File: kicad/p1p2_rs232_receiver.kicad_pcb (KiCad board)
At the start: 2 copper layers, 49 x 24.8 mm, 43 parts, among them J101 Conn_01x03_Female, J102 Conn_01x10_Female, U101 NCP1117-3.3_SOT223, U102 TEC2-1211WI, U103 LM4861

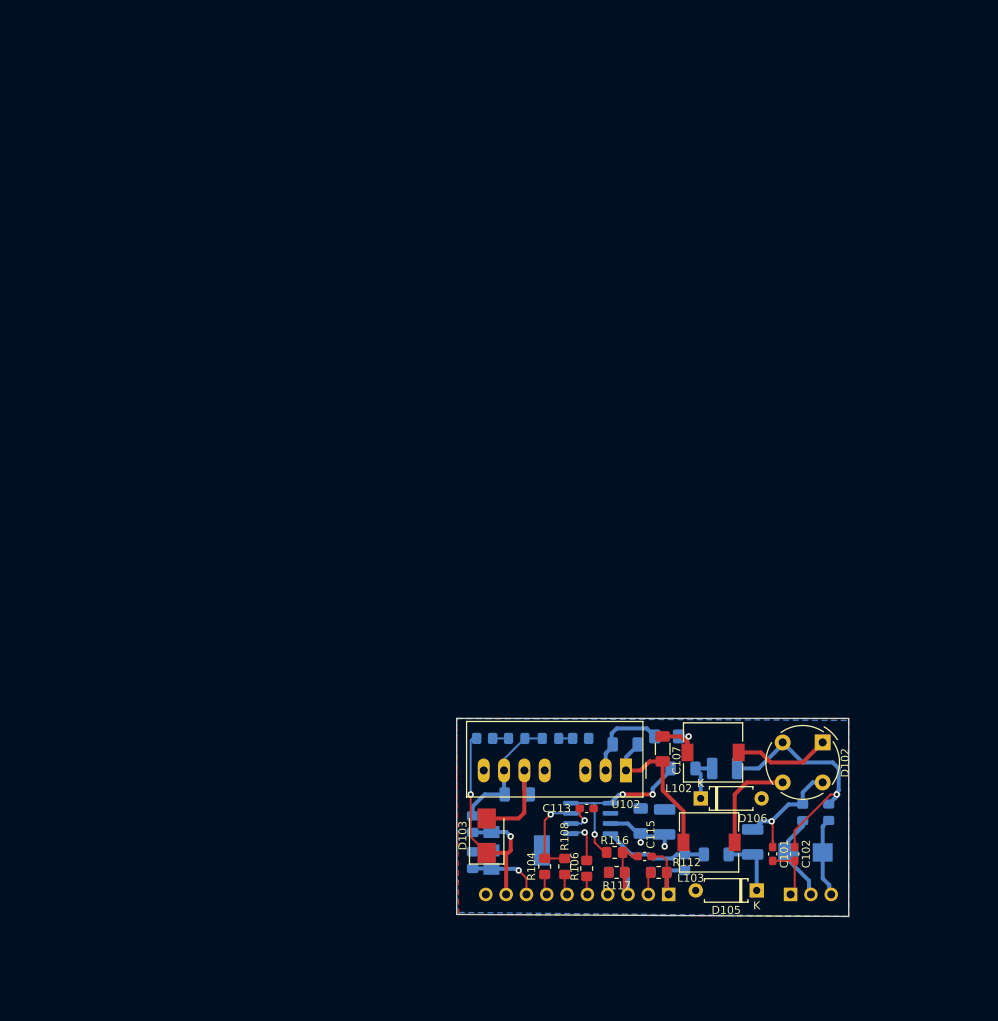
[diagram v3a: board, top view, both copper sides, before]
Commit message: kicad: Create a PI hat compatible P1/P2 modem
Create a P1/P2 transceiver as Rapsberry PI hat using some
analog components and a Raspberry PI Pico (RP2040).

Signed-off-by: Patrick Rudolph <rudolphpatrick05@gmail.com>
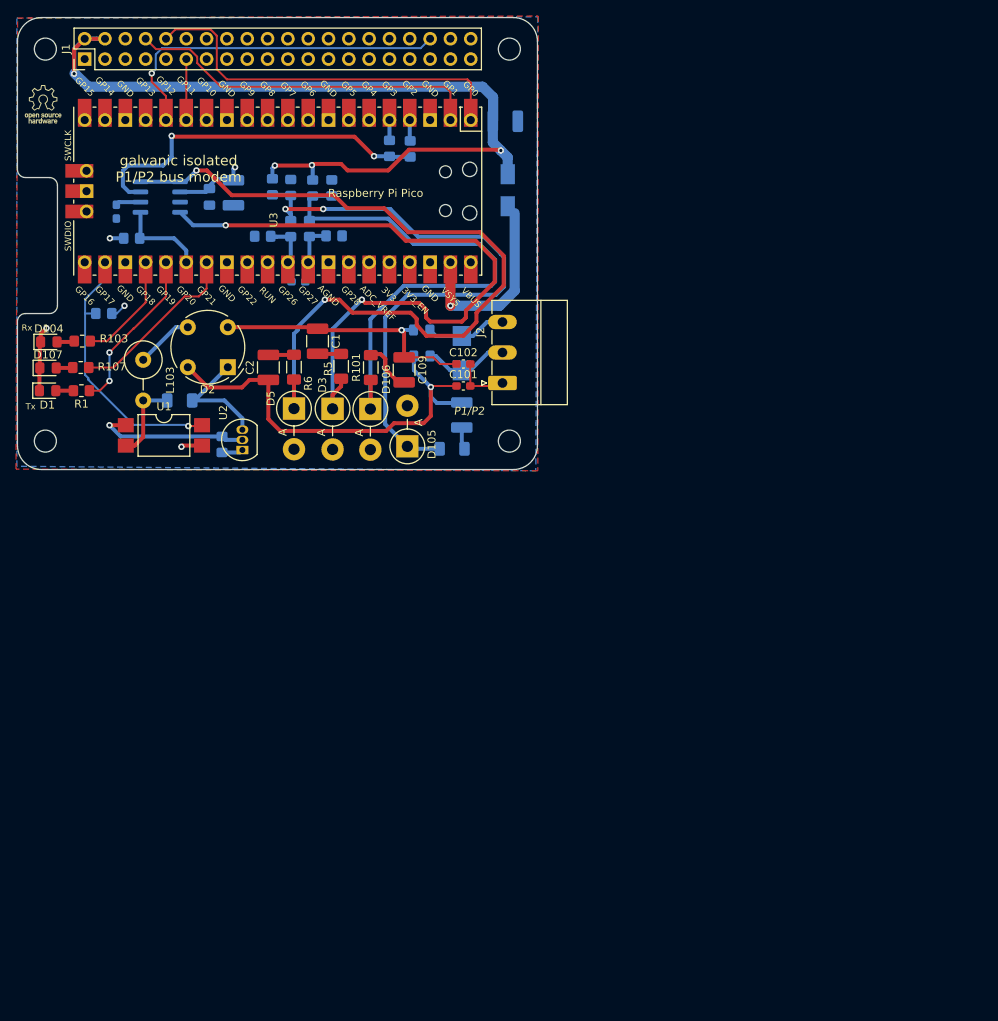
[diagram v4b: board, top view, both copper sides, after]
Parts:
- removed C103, C104: 10u, Capacitor_SMD:C_1206_3216Metric_Pad1.33x1.80mm_HandSolder
- removed C105: 100n, Capacitor_SMD:C_0805_2012Metric_Pad1.18x1.45mm_HandSolder
- removed C106: 2u, Capacitor_SMD:C_1206_3216Metric_Pad1.33x1.80mm_HandSolder
- removed D102: D_Bridge_+A-A, Diode_THT:Diode_Bridge_Round_D9.0mm
- removed D103: D_Schottky, Diode_SMD:D_SMB
- removed J101: Conn_01x03_Female, Connector_PinHeader_2.54mm:PinHeader_1x03_P2.54mm_Horizontal
- removed J102: Conn_01x10_Female, Connector_PinSocket_2.54mm:PinSocket_1x10_P2.54mm_Horizontal
- removed L101: 8u2, Inductor_SMD:L_1206_3216Metric_Pad1.42x1.75mm_HandSolder
- removed L102: PIS2812 1,0M, Inductor_SMD:L_7.3x7.3_H4.5
- removed R106: 2k2, Resistor_SMD:R_0805_2012Metric_Pad1.20x1.40mm_HandSolder
- removed U101: NCP1117-3.3_SOT223, Package_TO_SOT_SMD:SOT-223-3_TabPin2
- removed U102: TEC2-1211WI, Converter_DCDC:Converter_DCDC_TRACO_TMR-xxxx_THT
- added ?: , RPi_Hat:RPi_Hat_Mounting_Hole, F.Cu at (116.6, 35.6)
- added ?: , RPi_Hat:RPi_Hat_Mounting_Hole, F.Cu at (58.6, 84.6)
- added ?: , RPi_Hat:RPi_Hat_Mounting_Hole, F.Cu at (116.6, 84.6)
- added ?: , RPi_Hat:RPi_Hat_Mounting_Hole, F.Cu at (58.6, 35.6)
- added C1: 4u7, Capacitor_SMD:C_1210_3225Metric_Pad1.33x2.70mm_HandSolder, F.Cu at (92.6, 72.1)
- added C2: 4u7, Capacitor_SMD:C_1210_3225Metric_Pad1.33x2.70mm_HandSolder, F.Cu at (86.5, 75.4)
- added C3: 4u7, Capacitor_SMD:C_1210_3225Metric_Pad1.33x2.70mm_HandSolder, B.Cu at (116.1, 44.6)
- added D1: LED, LED_SMD:LED_0805_2012Metric_Pad1.15x1.40mm_HandSolder, F.Cu at (58.9, 78.3)
- added D2: D_Bridge_+A-A, Diode_THT:Diode_Bridge_Round_D9.0mm, F.Cu at (81.4, 75.3)
- added D3: ZF 3,6, Diode_THT:D_5W_P5.08mm_Vertical_AnodeUp, F.Cu at (94.5, 80.5)
- added D4: B120-E3, Diode_SMD:D_SMA, B.Cu at (116.4, 53.2)
- added D5: ZF 3,6, Diode_THT:D_5W_P5.08mm_Vertical_AnodeUp, F.Cu at (89.7, 80.5)
- added J1: Raspberry_Pi_2_3, Connector_PinHeader_2.54mm:PinHeader_2x20_P2.54mm_Vertical, F.Cu at (63.5, 36.8)
- added J2: PC MC_1,5_2-G-3.81, Connector_Phoenix_MC:PhoenixContact_MC_1,5_3-G-3.81_1x03_P3.81mm_Horizontal, F.Cu at (115.7, 77.3)
- added R1: 470, Resistor_SMD:R_0805_2012Metric_Pad1.20x1.40mm_HandSolder, F.Cu at (63.1, 78.3)
- added R2: 47k, Resistor_SMD:R_0805_2012Metric_Pad1.20x1.40mm_HandSolder, B.Cu at (69.4, 59.2)
- added R3: 4k7, Resistor_SMD:R_0805_2012Metric_Pad1.20x1.40mm_HandSolder, B.Cu at (65.9, 68.6)
- added R4: 240, Resistor_SMD:R_0805_2012Metric_Pad1.20x1.40mm_HandSolder, B.Cu at (80.7, 85.0)
- added R5: 2,2, Resistor_SMD:R_1206_3216Metric_Pad1.30x1.75mm_HandSolder, F.Cu at (95.6, 75.2)
- added R6: 2,2, Resistor_SMD:R_1206_3216Metric_Pad1.30x1.75mm_HandSolder, F.Cu at (89.7, 75.3)
- added R7: 12k2, Resistor_SMD:R_0805_2012Metric_Pad1.20x1.40mm_HandSolder, B.Cu at (85.8, 59.0)
- added R8: 12k2, Resistor_SMD:R_0805_2012Metric_Pad1.20x1.40mm_HandSolder, B.Cu at (94.7, 58.9)
- added U1: LTV-817S, Package_DIP:SMDIP-4_W9.53mm, F.Cu at (73.4, 83.9)
- added U2: LM317L_TO92, Package_TO_SOT_THT:TO-92_Inline, F.Cu at (83.2, 85.7)
- added U3: Pico, Pico:RPi_Pico_SMD_TH, F.Cu at (87.6, 53.3)
- C107: value 2u -> 1u; moved to B.Cu
- C109, D104, D107, R101, R107: moved to F.Cu
- C113, R104, R108: moved to B.Cu
- C115: value 6n8 -> 220p; moved to B.Cu
- D105, D106: footprint Diode_THT:D_A-405_P7.62mm_Horizontal -> Diode_THT:D_5W_P5.08mm_Vertical_AnodeUp
- L103: value PIS2812 1,0M -> L-HBCC 10M; footprint Inductor_SMD:L_7.3x7.3_H4.5 -> Inductor_THT:L_Axial_L14.0mm_D4.5mm_P5.08mm_Vertical_Fastron_LACC
- R102: value 4.7 -> 4,7
- R103: value 750 -> 470; moved to F.Cu
- R109, R114: value 220 -> 14k
- R110: value 150 -> 6k8
- R112, R117: value 220 -> 14k; moved to B.Cu
- R116: value 150 -> 6k8; moved to B.Cu
- moved R114 95.9 mm to (87.0, 52.8), turned to -90 degrees
- moved R109 95.9 mm to (92.0, 52.9), turned to -90 degrees
- moved C111 95.3 mm to (82.1, 53.5)
- moved C113 95.0 mm to (67.5, 55.9), turned to -90 degrees
- moved R112 94.8 mm to (94.4, 52.9), turned to 90 degrees
- moved R117 94.8 mm to (89.3, 52.9), turned to 90 degrees
- moved U103 94.5 mm to (72.9, 54.1)
- moved R110 93.3 mm to (89.3, 58.0)
- moved L103 93.0 mm to (70.8, 74.4), turned to -90 degrees
- moved R108 92.4 mm to (101.6, 48.0), turned to 90 degrees
- moved R104 91.3 mm to (104.2, 48.1), turned to -90 degrees
- moved C112 89.2 mm to (79.1, 54.1)
- moved R116 86.8 mm to (91.6, 58.0), turned to 90 degrees
- moved C115 83.9 mm to (90.2, 64.7)
- moved L104 78.9 mm to (105.6, 70.7), turned to 180 degrees
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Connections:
- D105 pad 1: Net-(C110-Pad2) -> Net-(D105-Pad1)
- D106 pad 1: Net-(C109-Pad2) -> Net-(D106-Pad1)
- R101 pad 1: /A -> Net-(D106-Pad1)
- R102 pad 1: /B -> Net-(D105-Pad1)
- R103 pad 1: +5V -> /LED_RX
- R107 pad 1: +3V3 -> /PWR_LED
- R109 pad 1: +3V3 -> +5V
- R109 pad 2: /ADC_B -> Net-(D106-Pad1)
- R110 pad 1: /ADC_B -> /ADC_A
- R110 pad 2: /B -> Net-(D105-Pad1)
- R112 pad 1: /ADC_B -> Net-(D106-Pad1)
- R114 pad 1: +3V3 -> +5V
- R114 pad 2: /ADC_A -> Net-(D105-Pad1)
- R116 pad 1: /ADC_A -> /ADC_B
- R116 pad 2: /A -> Net-(D106-Pad1)
- R117 pad 1: /ADC_A -> Net-(D105-Pad1)
- U103 pad 1: Net-(R106-Pad1) -> /SHUTDOWN
- U103 pad 4: /A -> Net-(U103-Pad4)
- U103 pad 5: /A -> Net-(U103-Pad4)
- U103 pad 8: /B -> Net-(U103-Pad8)
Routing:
- net Net-(U103-Pad4): track 0.00 -> 101.0 mm, vias 0 -> 2
- net Net-(U103-Pad8): track 0.00 -> 84.8 mm, vias 0 -> 2
- net +5V: track 30.8 -> 113.4 mm, vias 2 -> 4
- net Net-(D105-Pad1): track 0.00 -> 77.9 mm, vias 0 -> 2
- net Net-(D106-Pad1): track 0.00 -> 66.6 mm
- net /TX: track 0.00 -> 48.5 mm
- net /RX: track 0.00 -> 44.8 mm
- net /CTS: track 0.00 -> 44.5 mm, vias 0 -> 1
- net Net-(C101-Pad1): track 15.3 -> 55.2 mm
- net /CARRIER: track 0.00 -> 33.9 mm, vias 0 -> 1
- net Net-(R104-Pad2): track 11.0 -> 44.8 mm, vias 1 -> 2
- net GND: track 39.7 -> 10.8 mm, vias 3 -> 2
- net Net-(D4-Pad1): track 0.00 -> 25.2 mm, vias 0 -> 1
- net /PWR_LED: track 0.00 -> 22.1 mm
- net /A: track 21.5 -> 0.00 mm, vias 3 -> 0
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- added copper zone on F.Cu, net +3V3
- added copper zone on B.Cu, net GND
- removed copper zone on B.Cu, net +3V3
- removed copper zone on F.Cu, net GND
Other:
- board size 49 x 24.8 mm -> 65 x 56.5 mm
- net class Default removed
- board text added: "Dimensions taken from https://github.com/raspberrypi/hats/blob/master/hat-board-mechanical.pdf"
- board text added: "P1/P2"
- board text added: "Raspberry Pi Pico"
- board text added: "Rx"
- board text added: "Tx"
- board text added: "galvanic isolated P1/P2 bus modem"
- board text removed: "*"

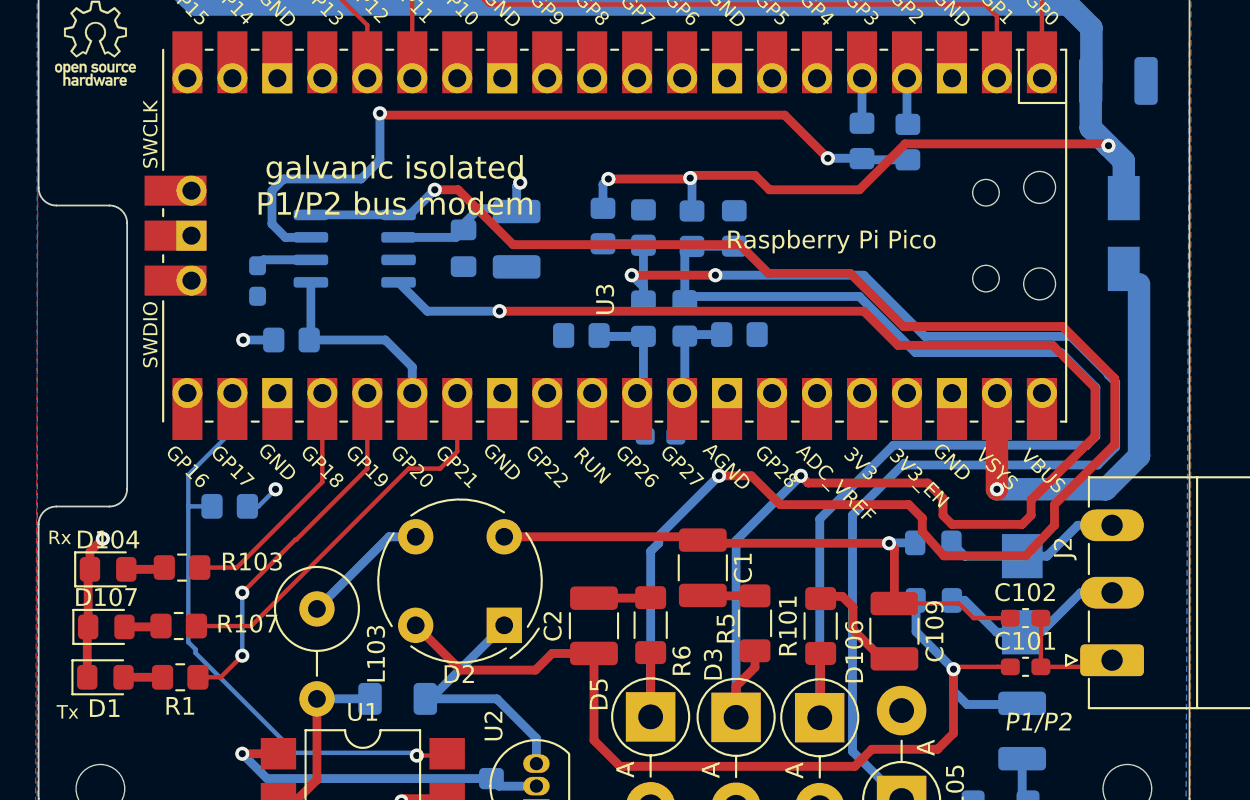
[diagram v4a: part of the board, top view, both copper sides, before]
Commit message: kicad: Minor fixes
Signed-off-by: Patrick Rudolph <rudolphpatrick05@gmail.com>
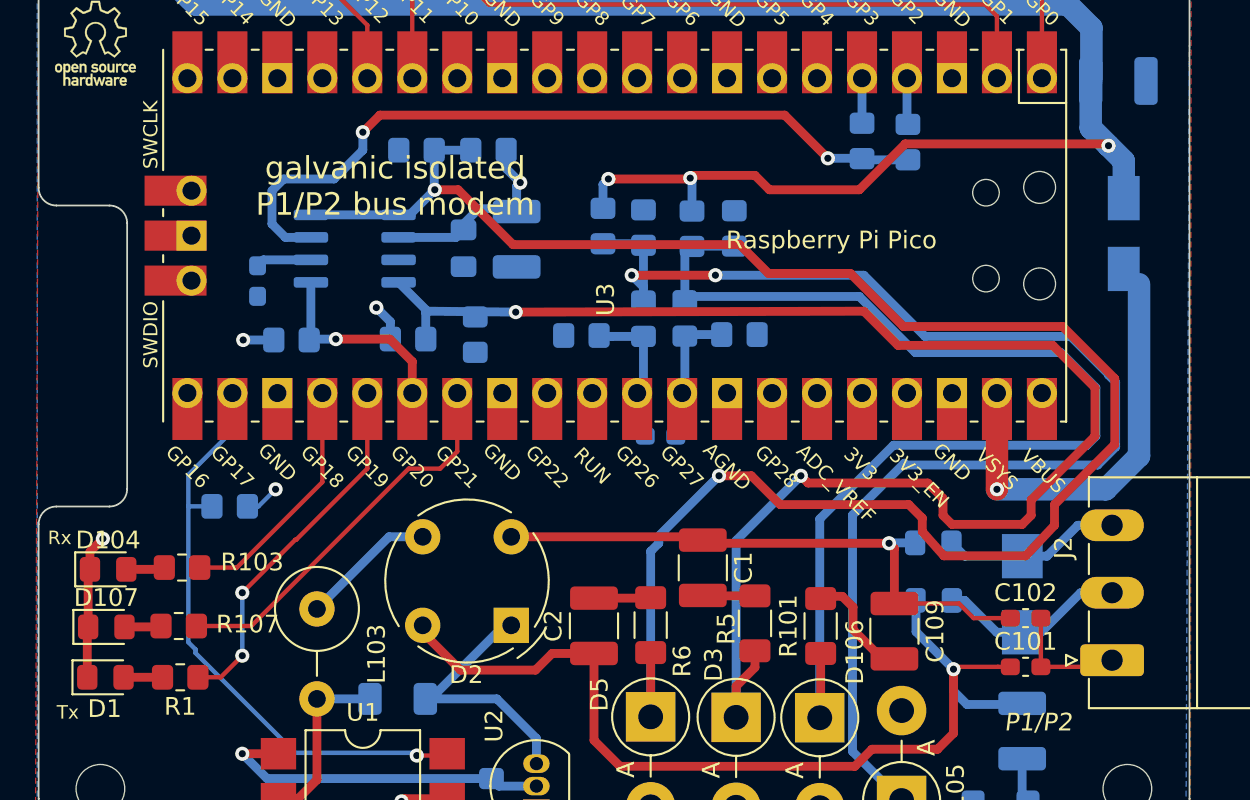
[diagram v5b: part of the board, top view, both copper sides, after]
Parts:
- added R10: 22k, Resistor_SMD:R_0805_2012Metric_Pad1.20x1.40mm_HandSolder, B.Cu at (76.4, 48.5)
- added R11: 22k, Resistor_SMD:R_0805_2012Metric_Pad1.20x1.40mm_HandSolder, B.Cu at (76.0, 59.2)
- added R12: 22k, Resistor_SMD:R_0805_2012Metric_Pad1.20x1.40mm_HandSolder, B.Cu at (79.8, 58.9)
- added R9: 22k, Resistor_SMD:R_0805_2012Metric_Pad1.20x1.40mm_HandSolder, B.Cu at (80.5, 48.5)
- L103: value L-HBCC 10M -> L-XHBCC 100M
- moved D2 0.40 mm to (81.8, 75.3)
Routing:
- net Net-(D5-Pad1): track 101.0 -> 105.3 mm
- net +3V3: track 13.1 -> 17.4 mm, vias 3 -> 4
- net Net-(D3-Pad1): track 84.8 -> 86.4 mm
- net Net-(R104-Pad2): track 44.8 -> 43.7 mm
- net /SHUTDOWN: track 11.2 -> 11.4 mm, vias 0 -> 1
